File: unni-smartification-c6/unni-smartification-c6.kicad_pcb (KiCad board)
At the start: 4 copper layers, 83.3 x 65 mm, 74 parts, among them J1 USB-C (replacement daughterbo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, J10 Conn_01x06, J2 Li-Ion 1S JST-PH, J3 Conn_01x06, J4 UNNI DC / battery input - AC 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, J5 Conn_01x02, J6 Conn_01x05, Q1 AO3401A, Q10 AO3400A touch emulator, Q2 AO3401A, Q3 AO3400A, Q4 AO3400A, SW1 RESET, SW2 BOOT, U1 MCP73831T-2ACI/OT, U10 ESP32-C6-MINI-1, U2 TPS63031DSK, U3 TPS613222ADBZ (5V), U4 TPD2E009DBZR

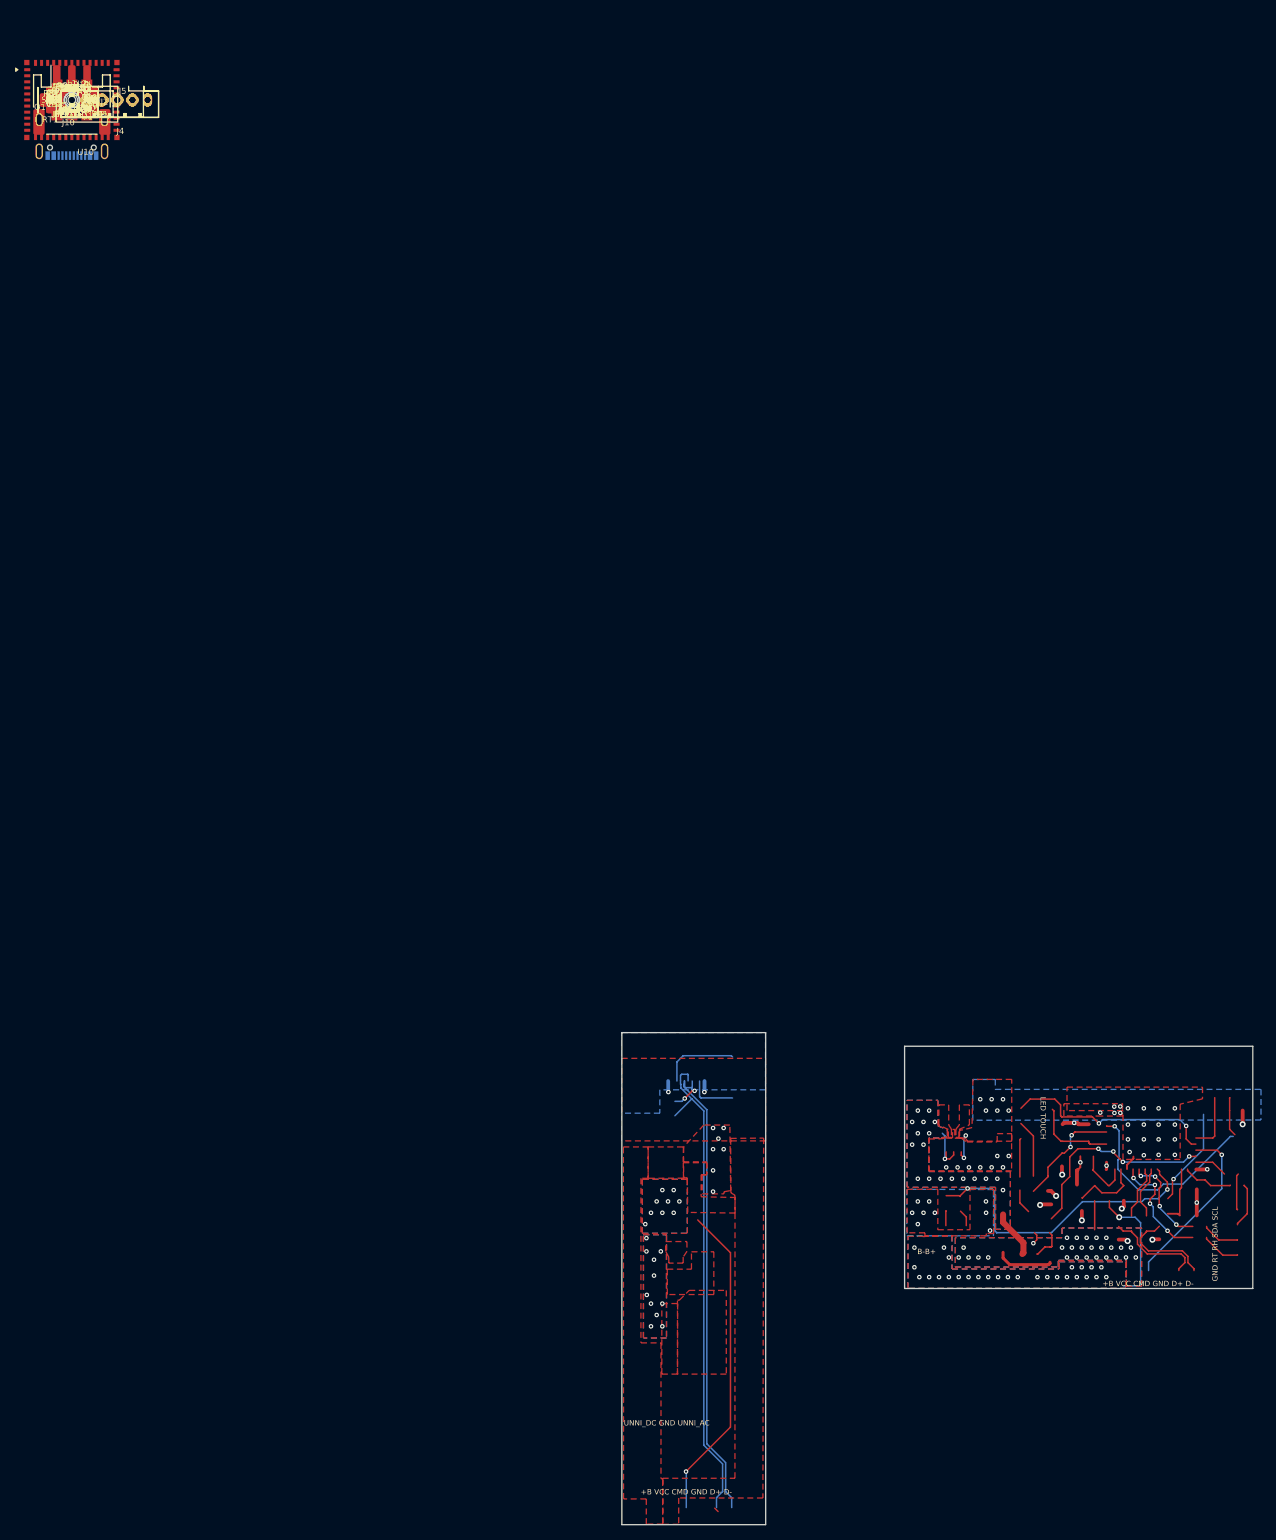
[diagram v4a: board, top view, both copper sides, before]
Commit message: Prepare Rev A prototype and add PCBWay sponsorship
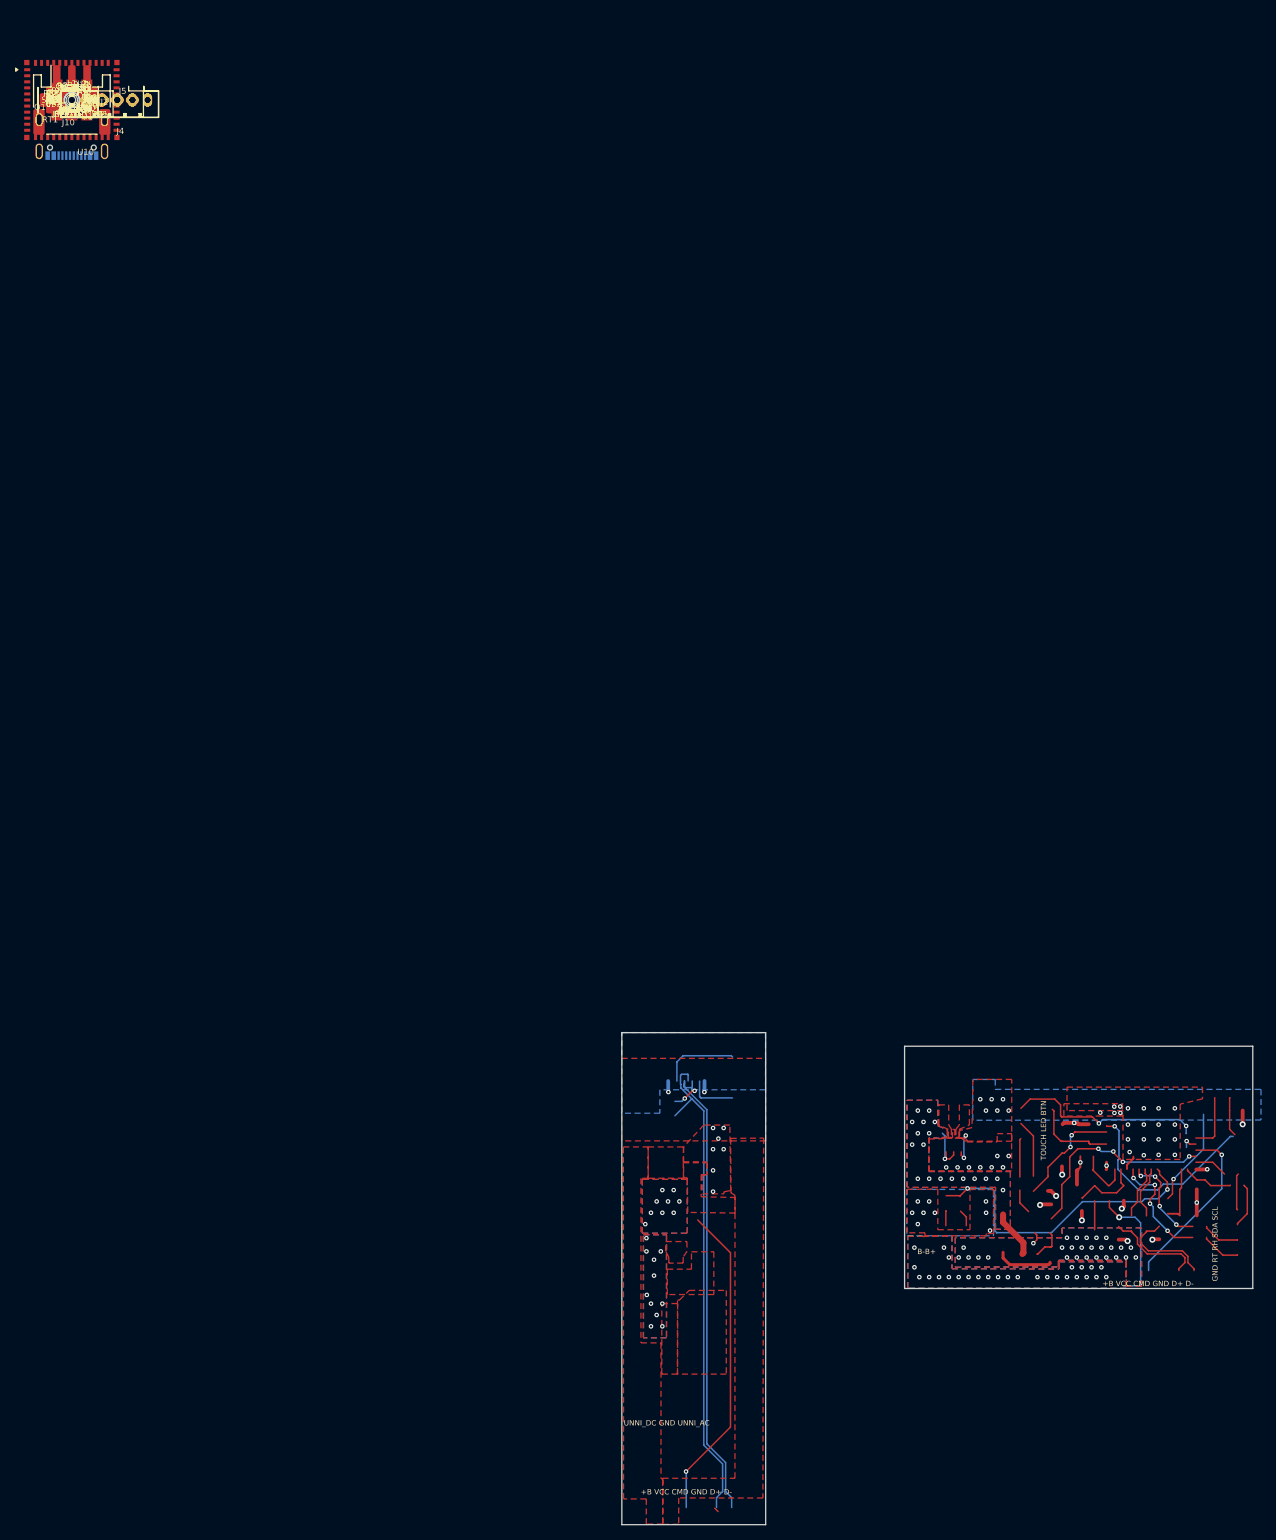
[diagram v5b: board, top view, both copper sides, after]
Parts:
- added R24: 10K, Resistor_SMD:R_0603_1608Metric_Pad0.98x0.95mm_HandSolder, B.Cu at (0.00, 0.00)
- C32: value 220pF DNP -> 220pF
- J5: value Conn_01x02 -> Conn_01x03
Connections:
- U10 pad 28: CONN_BTN -> Net-(U10-IO22)
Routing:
- net CONN_BTN: track 28.3 -> 26.1 mm
- net Net-(U10-IO22): track 0.00 -> 2.23 mm, vias 0 -> 1
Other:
- board text added: "TOUCH LED BTN"
- board text removed: "LED TOUCH"
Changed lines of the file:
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@@
 			(net "unconnected-(U10-IO8-Pad22)")
 			(pinfunction "IO8_22")
-			(pintype "bidirectional")
+			(pintype "bidirectional+no_connect")
 		)
 		(pad "23" smd rect
@@
 			(size 0.8 0.4)
 			(layers "F.Cu" "F.Mask" "F.Paste")
-			(net "CONN_BTN")
+			(net "Net-(U10-IO22)")
 			(pinfunction "IO22_28")
 			(pintype "bidirectional")
@@
 		(tags "connector JST PH vertical")
 		(property "Reference" "J5"
-			(at 6.7 -1.18 180)
+			(at 6.7 -1.18 360)
 			(layer "F.SilkS")
 			(effects
@@
 			)
 		)
-		(property "Value" "Conn_01x02"
+		(property "Value" "Conn_01x03"
 			(at 2 4 90)
 			(layer "F.Fab")
@@
 		(duplicate_pad_numbers_are_jumpers no)
 		(fp_line
-			(start -2.36 -2.11)
-			(end -2.36 -0.86)
-			(stroke
-				(width 0.12)
-				(type solid)
-			)
-			(layer "F.SilkS")
-		)
-		(fp_line
-			(start -2.06 -0.5)
-			(end -1.45 -0.5)
-			(stroke
-				(width 0.12)
-				(type solid)
-			)
-			(layer "F.SilkS")
-		)
-		(fp_line
-			(start -2.06 0.8)
-			(end -1.45 0.8)
-			(stroke
-				(width 0.12)
-				(type solid)
-			)
-			(layer "F.SilkS")
-		)
-		(fp_line
 			(start -1.45 -1.2)
 			(end -1.45 2.3)
@@
 		)
 		(fp_line
-			(start -1.11 -2.11)
-			(end -2.36 -2.11)
-			(stroke
-				(width 0.12)
-				(type solid)
-			)
-			(layer "F.SilkS")
-		)
-		(fp_line
-			(start -0.6 -2.01)
-			(end -0.6 -1.81)
-			(stroke
-				(width 0.12)
-				(type solid)
-			)
-			(layer "F.SilkS")
-		)
-		(fp_line
-			(start -0.3 -2.01)
-			(end -0.6 -2.01)
-			(stroke
-				(width 0.12)
-				(type solid)
-			)
-			(layer "F.SilkS")
-		)
-		(fp_line
-			(start -0.3 -1.91)
-			(end -0.6 -1.91)
-			(stroke
-				(width 0.12)
-				(type solid)
-			)
-			(layer "F.SilkS")
-		)
-		(fp_line
-			(start -0.3 -1.81)
-			(end -0.3 -2.01)
-			(stroke
-				(width 0.12)
-				(type solid)
-			)
-			(layer "F.SilkS")
-		)
-		(fp_line
 			(start 0.5 -1.81)
 			(end 0.5 -1.2)
@@
 			(layer "F.SilkS")
 		)
-		(fp_line
-			(start 6.06 -0.5)
-			(end 5.45 -0.5)
-			(stroke
-				(width 0.12)
-				(type solid)
-			)
-			(layer "F.SilkS")
-		)
-		(fp_line
-			(start 6.06 0.8)
-			(end 5.45 0.8)
-			(stroke
-				(width 0.12)
-				(type solid)
-			)
-			(layer "F.SilkS")
-		)
-		(fp_rect
-			(start -2.06 -1.81)
-			(end 6.06 2.91)
-			(stroke
-				(width 0.12)
-				(type solid)
-			)
-			(fill no)
-			(layer "F.SilkS")
-		)
 		(fp_rect
 			(start -2.45 -2.2)
@@
 		(tags "capacitor handsolder")
 		(property "Reference" "C32"
-			(at -2.28 0.51 0)
+			(at -2.41 0.51 0)
 			(layer "F.SilkS")
 			(effects
@@
 			)
 		)
-		(property "Value" "220pF DNP"
+		(property "Value" "220pF"
 			(at 0 1.43 90)
 			(layer "F.Fab")
@@
 		)
 	)
+	(footprint "Resistor_SMD:R_0603_1608Metric_Pad0.98x0.95mm_HandSolder"
+		(layer "B.Cu")
+		(transform
+			(translate 147.235 137.455)
+			(rotate 90)
+			(scale 1 1)
+		)
+		(descr "Resistor SMD 0603 (1608 Metric), square (rectangular) end terminal, IPC-7351 nominal with elongated pad for handsoldering. (Body size source: IPC-SM-782 page 72, https://www.pcb-3d.com/wordpress/wp-content/uploads/ipc-sm-782a_amendment_1_and_2.pdf)")
+		(tags "resistor handsolder")
+		(property "Reference" "R24"
+			(at 0 1.43 90)
+			(layer "B.SilkS")
+			(effects
+				(font
+					(size 1 1)
+					(thickness 0.15)
+				)
+				(justify mirror)
+			)
+		)
+		(property "Value" "10K"
+			(at 0 -1.43 90)
+			(layer "B.Fab")
+			(effects
+				(font
+					(size 1 1)
+					(thickness 0.15)
+				)
+				(justify mirror)
+			)
+		)
+		(property "Datasheet" ""
+			(at 0 0 90)
+			(layer "B.Fab")
+			(hide yes)
+			(effects
+				(font
+					(size 1.27 1.27)
+				)
+				(justify mirror)
+			)
+		)
+		(property "Description" ""
+			(at 0 0 90)
+			(layer "B.Fab")
+			(hide yes)
+			(effects
+				(font
+					(size 1.27 1.27)
+				)
+				(justify mirror)
+			)
+		)
+		(property "KiLib_Generator" "SMD_2terminal_chip_molded"
+			(at 0 0 90)
+			(layer "B.SilkS")
+			(hide yes)
+			(effects
+				(font
+					(size 1 1)
+					(thickness 0.15)
+				)
+				(justify mirror)
+			)
+		)
+		(property ki_fp_filters "R_*")
+		(sheetname "/ESP32-C6 + Auxiliary/")
+		(sheetfile "02_esp_aux.kicad_sch")
+		(units
+			(unit
+				(name "A")
+				(pins "1" "2")
+			)
+		)
+		(attr smd)
+		(duplicate_pad_numbers_are_jumpers no)
+		(fp_line
+			(start -0.254724 -0.5225)
+			(end 0.254724 -0.5225)
+			(stroke
+				(width 0.12)
+				(type solid)
+			)
+			(layer "B.SilkS")
+		)
+		(fp_line
+			(start -0.254724 0.5225)
+			(end 0.254724 0.5225)
+			(stroke
+				(width 0.12)
+				(type solid)
+			)
+			(layer "B.SilkS")
+		)
+		(fp_rect
+			(start -1.65 0.73)
+			(end 1.65 -0.73)
+			(stroke
+				(width 0.05)
+				(type solid)
+			)
+			(fill no)
+			(layer "B.CrtYd")
+		)
+		(fp_rect
+			(start -0.8 0.4125)
+			(end 0.8 -0.4125)
+			(stroke
+				(width 0.1)
+				(type solid)
+			)
+			(fill no)
+			(layer "B.Fab")
+		)
+		(fp_text user "${REFERENCE}"
+			(at 0 0 90)
+			(layer "B.Fab")
+			(effects
+				(font
+					(size 0.4 0.4)
+					(thickness 0.06)
+				)
+				(justify mirror)
+			)
+		)
+		(pad "1" smd roundrect
+			(at -0.9125 0 90)
+			(size 0.975 0.95)
+			(layers "B.Cu" "B.Mask" "B.Paste")
+			(roundrect_rratio 0.25)
+			(net "Net-(U10-IO22)")
+			(pintype "passive")
+		)
+		(pad "2" smd roundrect
+			(at 0.9125 0 90)
+			(size 0.975 0.95)
+			(layers "B.Cu" "B.Mask" "B.Paste")
+			(roundrect_rratio 0.25)
+			(net "CONN_BTN")
+			(pintype "passive")
+		)
+		(embedded_fonts no)
+		(model "${KICAD10_3DMODEL_DIR}/Resistor_SMD.3dshapes/R_0603_1608Metric.step"
+			(offset
+				(xyz 0 0 0)
+			)
+			(scale
+				(xyz 1 1 1)
+			)
+			(rotate
+				(xyz 0 0 0)
+			)
+		)
+	)
 	(gr_line
 		(start 72.65 123.2)
@@
 		)
 	)
-	(gr_text "GND RT RH SDA SCL"
-		(at 151.43 156.07 90)
+	(gr_text "TOUCH LED BTN"
+		(at 128.78 140.06 90)
 		(layer "F.SilkS" knockout)
 		(effects
@@
 		)
 	)
-	(gr_text "LED TOUCH"
-		(at 127.88 131.67 270)
+	(gr_text "GND RT RH SDA SCL"
+		(at 151.43 156.07 90)
 		(layer "F.SilkS" knockout)
 		(effects
@@
 	)
 	(segment
-		(start 148.481098 137.925)
-		(end 147.881098 137.925)
-		(width 0.2)
-		(layer "F.Cu")
-		(net "CONN_BTN")
-	)
-	(segment
 		(start 126.58 131.98)
 		(end 129.84 131.98)
@@
 	)
 	(segment
-		(start 147.2 137.243902)
-		(end 147.2 135.53)
-		(width 0.2)
-		(layer "F.Cu")
-		(net "CONN_BTN")
-	)
-	(segment
-		(start 147.881098 137.925)
-		(end 147.2 137.243902)
-		(width 0.2)
-		(layer "F.Cu")
-		(net "CONN_BTN")
-	)
-	(segment
 		(start 130.61 134.18)
 		(end 130.77 134.34)
@@
 	)
 	(segment
+		(start 147.2 136.5075)
+		(end 147.235 136.5425)
+		(width 0.2)
+		(layer "B.Cu")
+		(net "CONN_BTN")
+	)
+	(segment
+		(start 147.2 135.53)
+		(end 147.2 136.5075)
+		(width 0.2)
+		(layer "B.Cu")
+		(net "CONN_BTN")
+	)
+	(segment
 		(start 136.17 134.69)
 		(end 146.36 134.69)
@@
 		(net "Net-(J1-CC1)")
 	)
+	(segment
+		(start 147.655 137.925)
+		(end 148.481098 137.925)
+		(width 0.2)
+		(layer "F.Cu")
+		(net "Net-(U10-IO22)")
+	)
+	(segment
+		(start 147.26 137.53)
+		(end 147.655 137.925)
+		(width 0.2)
+		(layer "F.Cu")
+		(net "Net-(U10-IO22)")
+	)
+	(via
+		(at 147.26 137.53)
+		(size 0.6)
+		(drill 0.3)
+		(layers "F.Cu" "B.Cu")
+		(net "Net-(U10-IO22)")
+	)
+	(segment
+		(start 147.235 138.3675)
+		(end 147.235 137.555)
+		(width 0.2)
+		(layer "B.Cu")
+		(net "Net-(U10-IO22)")
+	)
+	(segment
+		(start 147.235 137.555)
+		(end 147.26 137.53)
+		(width 0.2)
+		(layer "B.Cu")
+		(net "Net-(U10-IO22)")
+	)
 	(zone

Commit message: Add BOM Metadata, iBom, fix validation, pcbway order
this is the state the PCBs were ordered at PCBWay.com

Thank you PCBWay for sponsoring the boards for this ridicoulus project!
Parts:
- D3: value SS14 USB -> UNNI_AC -> SS14
- D4: value SS14 BOOST -> UNNI_AC -> SS14
- J1: value USB-C (replacement daughterboard) -> UJ20-C-H-G-SMT-1-P16-TR
- J10, J3: value Conn_01x06 -> B6B-PH-K-S
- J2: value Li-Ion 1S JST-PH -> B2B-PH-K-S
- J4: value UNNI DC / battery input - AC / 5V Input -> S3B-PH-SM4-TB
- J5: value Conn_01x03 -> B3B-PH-K-S
- J6: value Conn_01x05 -> B5B-PH-K-S
- Q10: value AO3400A touch emulator -> AO3400A
- RT1: value 10k NTC @25C -> NTCC-10K
- U1: value MCP73831T-2ACI/OT -> MCP73831
- U10: value ESP32-C6-MINI-1 -> ESP32-C6-MINI-1-N4
- U2: value TPS63031DSK -> TPS63031
- U3: value TPS613222ADBZ (5V) -> TPS613222A
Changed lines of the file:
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@@
 			)
 		)
-		(property "Value" "TPS63031DSK"
+		(property "Value" "TPS63031"
 			(at 0 2.2 90)
 			(layer "F.Fab")
@@
 			)
 		)
-		(property "Value" "Conn_01x05"
+		(property "Value" "B5B-PH-K-S"
 			(at 4 4 90)
 			(layer "F.Fab")
@@
 			)
 		)
-		(property "Value" "UNNI DC / battery input - AC / 5V Input"
+		(property "Value" "S3B-PH-SM4-TB"
 			(at 0 5.8 0)
 			(layer "F.Fab")
@@
 			)
 		)
-		(property "Value" "ESP32-C6-MINI-1"
+		(property "Value" "ESP32-C6-MINI-1-N4"
 			(at 0 6.9 0)
 			(unlocked yes)
@@
 			)
 		)
-		(property "Value" "TPS613222ADBZ (5V)"
+		(property "Value" "TPS613222A"
 			(at 0 2.5 360)
 			(layer "F.Fab")
@@
 			)
 		)
-		(property "Value" "Conn_01x03"
+		(property "Value" "B3B-PH-K-S"
 			(at 2 4 90)
 			(layer "F.Fab")
@@
 			)
 		)
-		(property "Value" "SS14 USB -> UNNI_AC"
+		(property "Value" "SS14"
 			(at 0 2.6 0)
 			(layer "F.Fab")
@@
 			)
 		)
-		(property "Value" "Li-Ion 1S JST-PH"
+		(property "Value" "B2B-PH-K-S"
 			(at 1 4 0)
 			(layer "F.Fab")
@@
 			)
 		)
-		(property "Value" "AO3400A touch emulator"
+		(property "Value" "AO3400A"
 			(at 0 2.5 360)
 			(layer "F.Fab")
@@
 			)
 		)
-		(property "Value" "Conn_01x06"
+		(property "Value" "B6B-PH-K-S"
 			(at 5 4 360)
 			(layer "F.Fab")
@@
 			)
 		)
-		(property "Value" "MCP73831T-2ACI/OT"
+		(property "Value" "MCP73831"
 			(at 0 2.9 0)
 			(layer "F.Fab")
@@
 			)
 		)
-		(property "Value" "SS14 BOOST -> UNNI_AC"
+		(property "Value" "SS14"
 			(at 0 2.6 90)
 			(layer "F.Fab")
@@
 			)
 		)
-		(property "Value" "10k NTC @25C"
+		(property "Value" "NTCC-10K"
 			(at 1 4 90)
 			(layer "F.Fab")
@@
 			)
 		)
-		(property "Value" "Conn_01x06"
+		(property "Value" "B6B-PH-K-S"
 			(at 5 4 360)
 			(layer "F.Fab")
@@
 			)
 		)
-		(property "Value" "USB-C (replacement daughterboard)"
+		(property "Value" "UJ20-C-H-G-SMT-1-P16-TR"
 			(at 3.05375 -21.11625 90)
 			(layer "B.Fab")

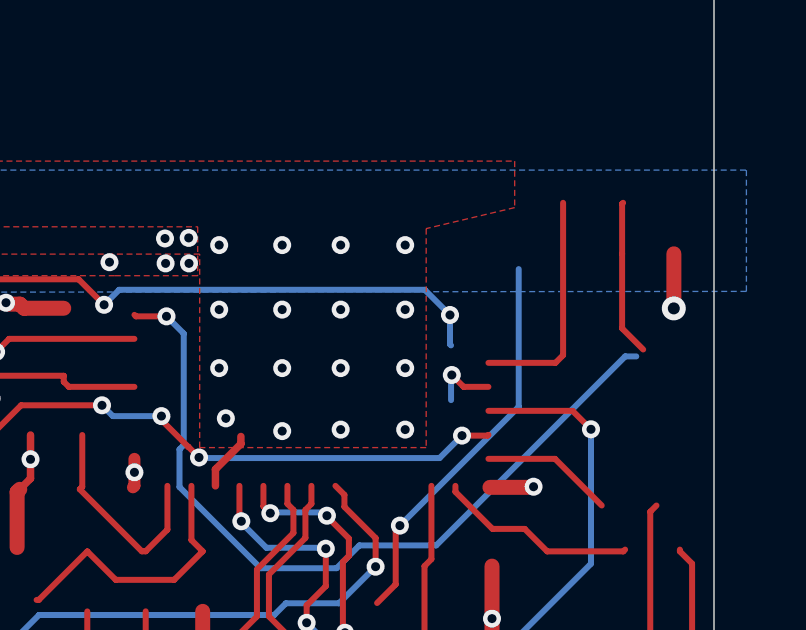
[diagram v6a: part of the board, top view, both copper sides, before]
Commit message: fix dangling via
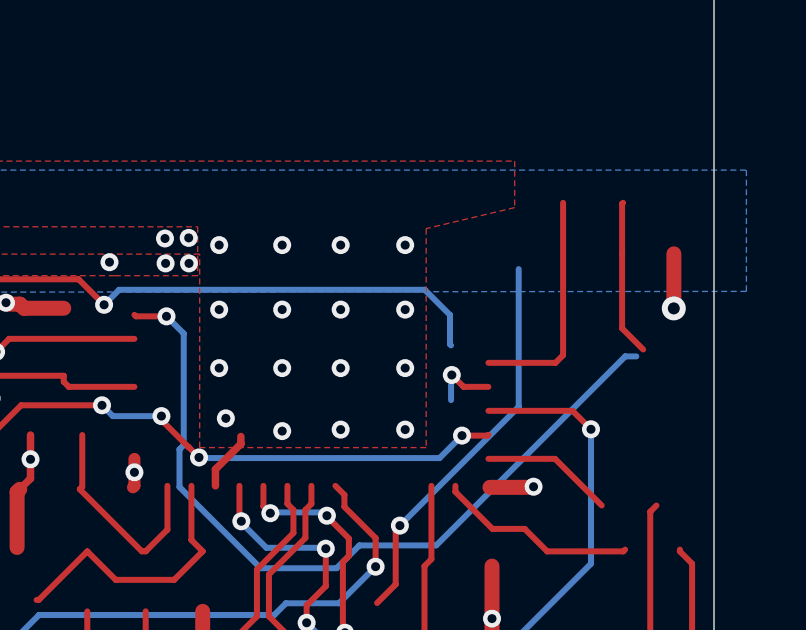
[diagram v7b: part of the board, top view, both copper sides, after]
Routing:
- net CONN_BTN: vias 2 -> 1
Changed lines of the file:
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@@
-	)
-	(via
-		(at 147.2 135.53)
-		(size 0.6)
-		(drill 0.3)
-		(layers "F.Cu" "B.Cu")
-		(net "CONN_BTN")
 	)
 	(via
